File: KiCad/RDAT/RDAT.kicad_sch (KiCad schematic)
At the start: 0 parts

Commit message: Add data from KiCAD and review
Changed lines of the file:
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@@
 	)
 	(sheet
-		(at 223.52 91.44)
+		(at 125.73 55.88)
 		(size 48.26 15.24)
 		(fields_autoplaced yes)
@@
 		)
 		(property "Sheetname" "usbC_Switcher"
-			(at 223.52 90.7284 0)
+			(at 125.73 55.1684 0)
 			(effects
 				(font
@@
 		)
 		(property "Sheetfile" "C_switcher.kicad_sch"
-			(at 223.52 107.2646 0)
+			(at 125.73 71.7046 0)
 			(effects
 				(font
@@
 	)
 	(sheet
-		(at 127 78.74)
+		(at 81.28 48.26)
 		(size 30.48 25.4)
 		(fields_autoplaced yes)
@@
 		)
 		(property "Sheetname" "LattePanda_mu"
-			(at 127 78.0284 0)
+			(at 81.28 47.5484 0)
 			(effects
 				(font
@@
 		)
 		(property "Sheetfile" "mu_cm.kicad_sch"
-			(at 127 104.7246 0)
+			(at 81.28 74.2446 0)
 			(effects
 				(font
@@
 	)
 	(sheet
-		(at 76.2 54.61)
+		(at 66.04 95.25)
 		(size 12.7 5.08)
 		(fields_autoplaced yes)
@@
 		)
 		(property "Sheetname" "VRM"
-			(at 76.2 53.8984 0)
+			(at 66.04 94.5384 0)
 			(effects
 				(font
@@
 		)
 		(property "Sheetfile" "vrm.kicad_sch"
-			(at 76.2 60.2746 0)
+			(at 66.04 100.9146 0)
 			(effects
 				(font
@@
 	)
 	(sheet
-		(at 226.06 125.73)
+		(at 114.3 87.63)
 		(size 40.64 20.32)
 		(fields_autoplaced yes)
@@
 		)
 		(property "Sheetname" "BMS"
-			(at 226.06 125.0184 0)
+			(at 114.3 86.9184 0)
 			(effects
 				(font
@@
 		)
 		(property "Sheetfile" "bms.kicad_sch"
-			(at 226.06 146.6346 0)
+			(at 114.3 108.5346 0)
 			(effects
 				(font

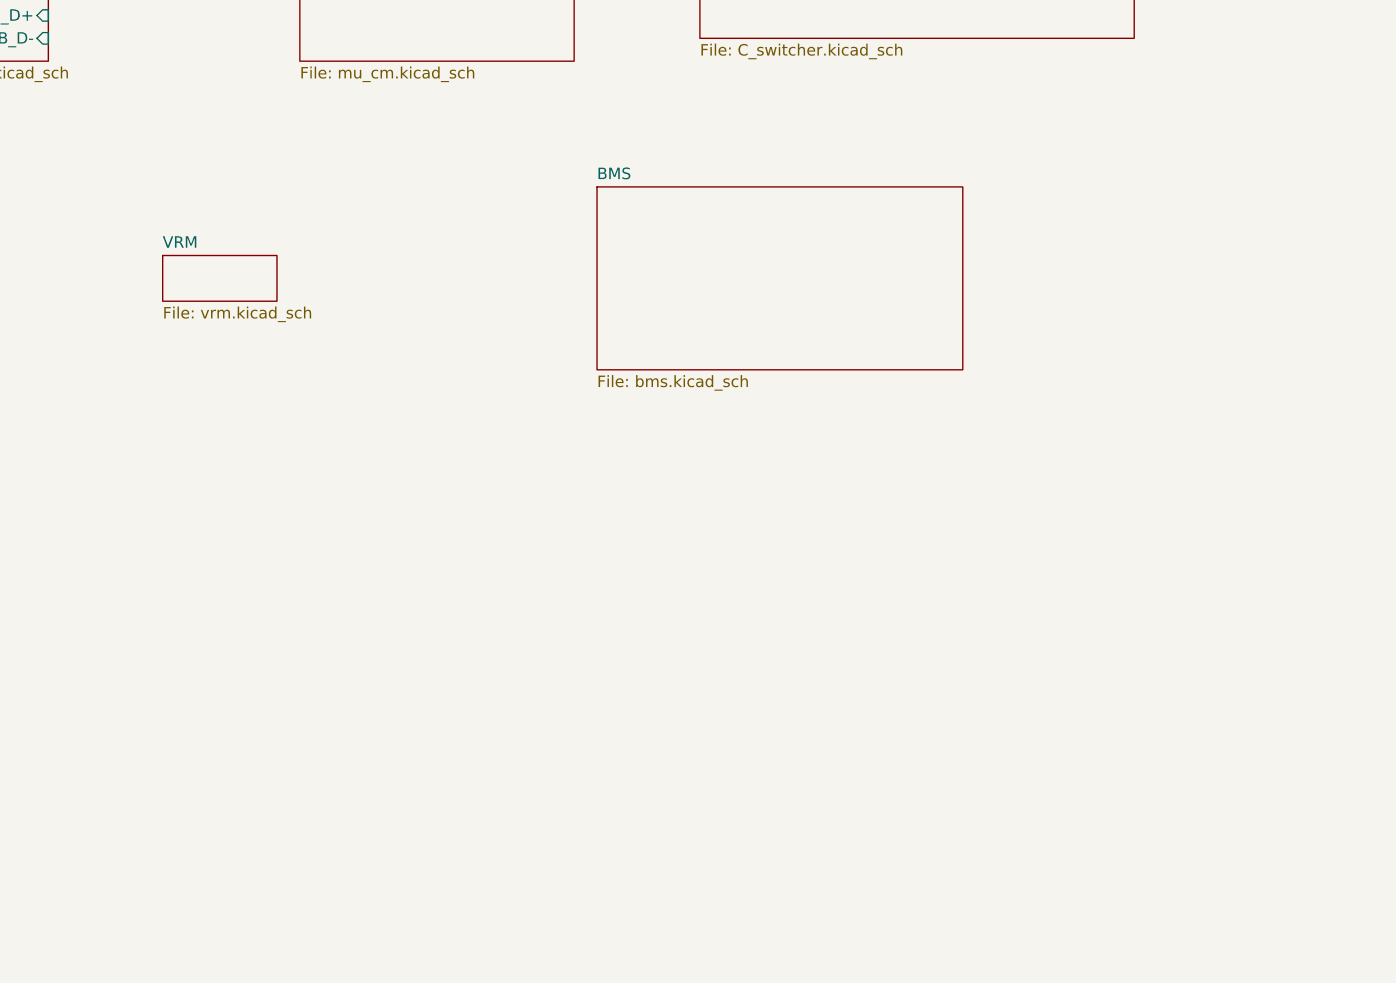
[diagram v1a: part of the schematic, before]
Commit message: BMS circuitry
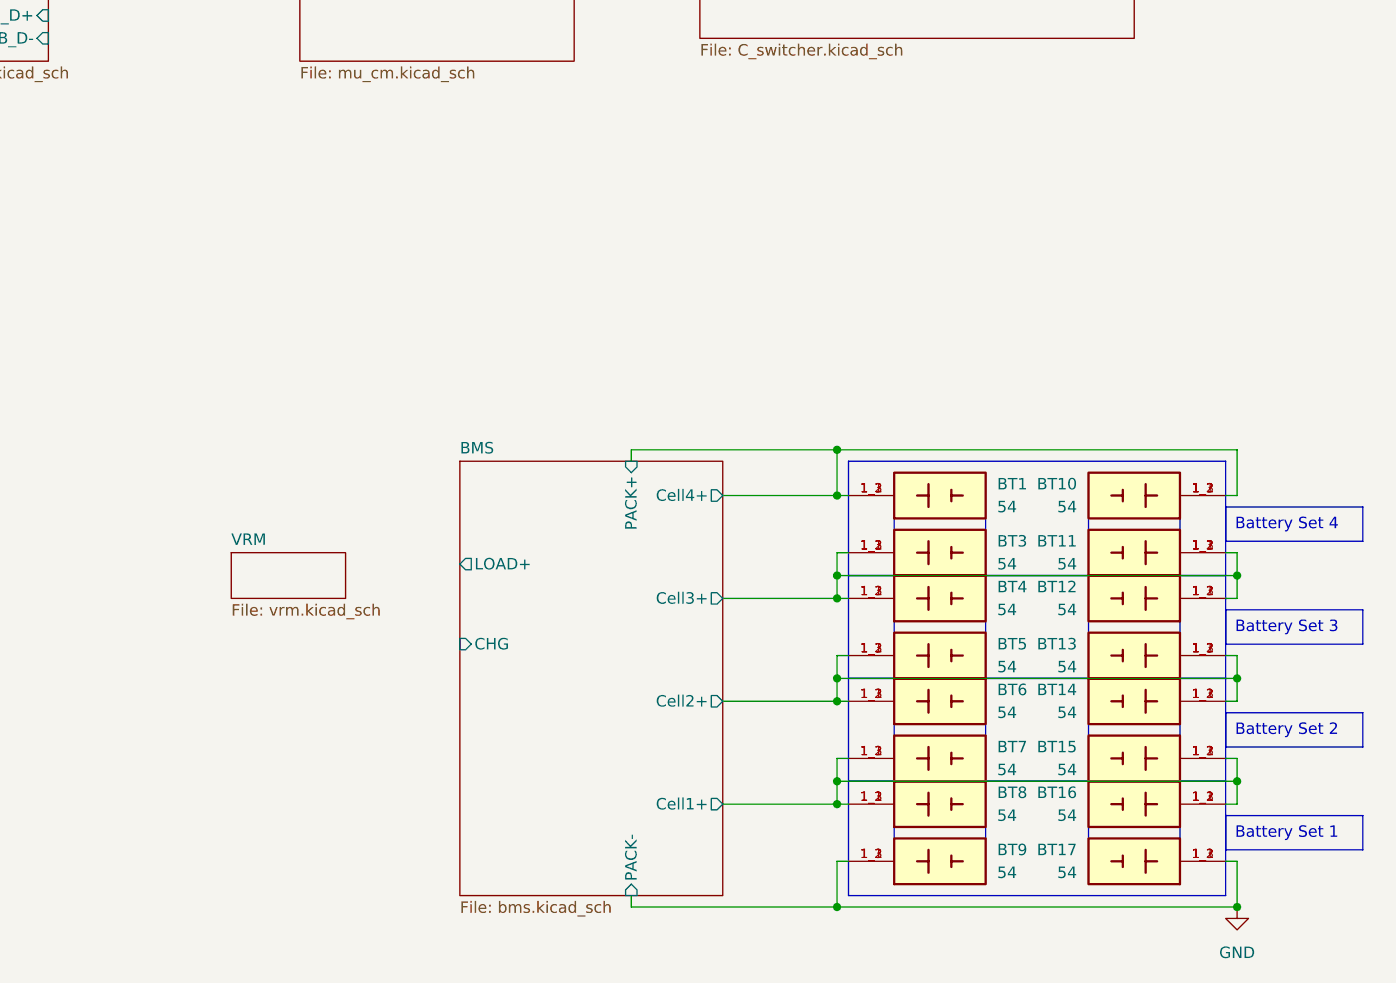
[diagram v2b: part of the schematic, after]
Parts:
- added BT1, BT10, BT11, BT12, BT13, BT14, BT15, BT16, BT17, BT3, BT4, BT5, BT6, BT7, BT8, BT9: 54, 54:BAT_54, symbol 54:54
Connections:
- new net BMS/Cell1+: BT15.1_1, BT15.1_2, BT15.1_3, BT16.1_1, BT16.1_2, BT16.1_3, BT7.1_1, BT7.1_2, BT7.1_3, BT8.1_1, BT8.1_2, BT8.1_3
- new net BMS/Cell2+: BT13.1_1, BT13.1_2, BT13.1_3, BT14.1_1, BT14.1_2, BT14.1_3, BT5.1_1, BT5.1_2, BT5.1_3, BT6.1_1, BT6.1_2, BT6.1_3
- new net BMS/Cell3+: BT11.1_1, BT11.1_2, BT11.1_3, BT12.1_1, BT12.1_2, BT12.1_3, BT3.1_1, BT3.1_2, BT3.1_3, BT4.1_1, BT4.1_2, BT4.1_3
- new net BMS/Cell4+: BT1.1_1, BT1.1_2, BT1.1_3, BT10.1_1, BT10.1_2, BT10.1_3
- new net GND: BT17.1_1, BT17.1_2, BT17.1_3, BT9.1_1, BT9.1_2, BT9.1_3
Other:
- sheet BMS ports: added CHG, Cell1+, Cell2+, Cell3+, Cell4+, LOAD+, PACK+, PACK-; removed none

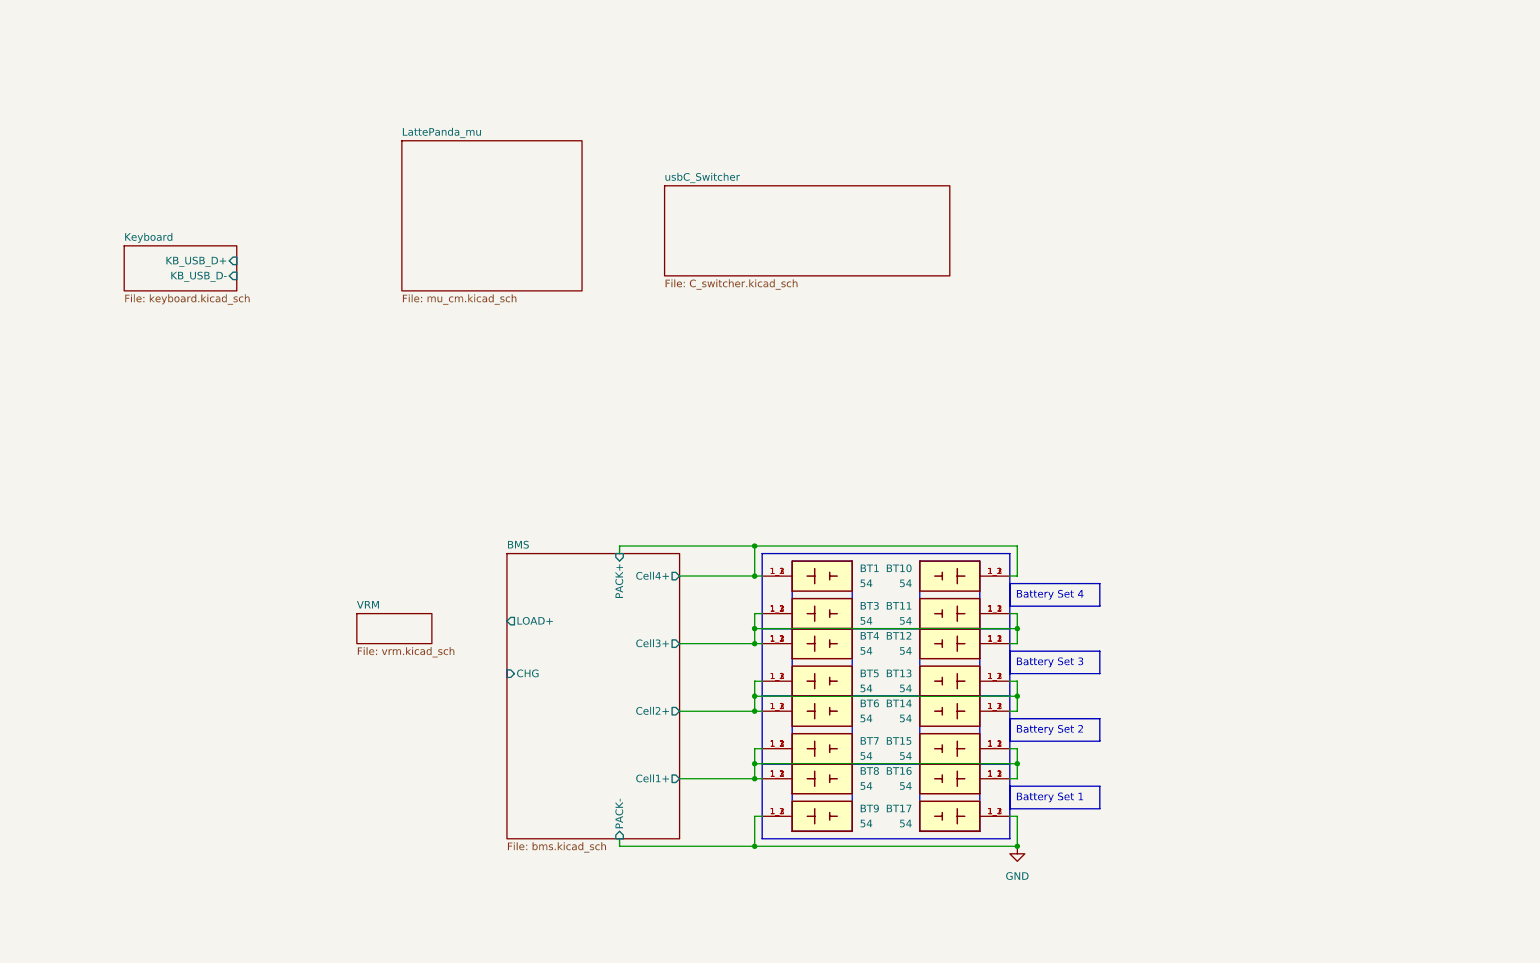
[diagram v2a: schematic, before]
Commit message: Added kicad USBC controller and connected VBUS
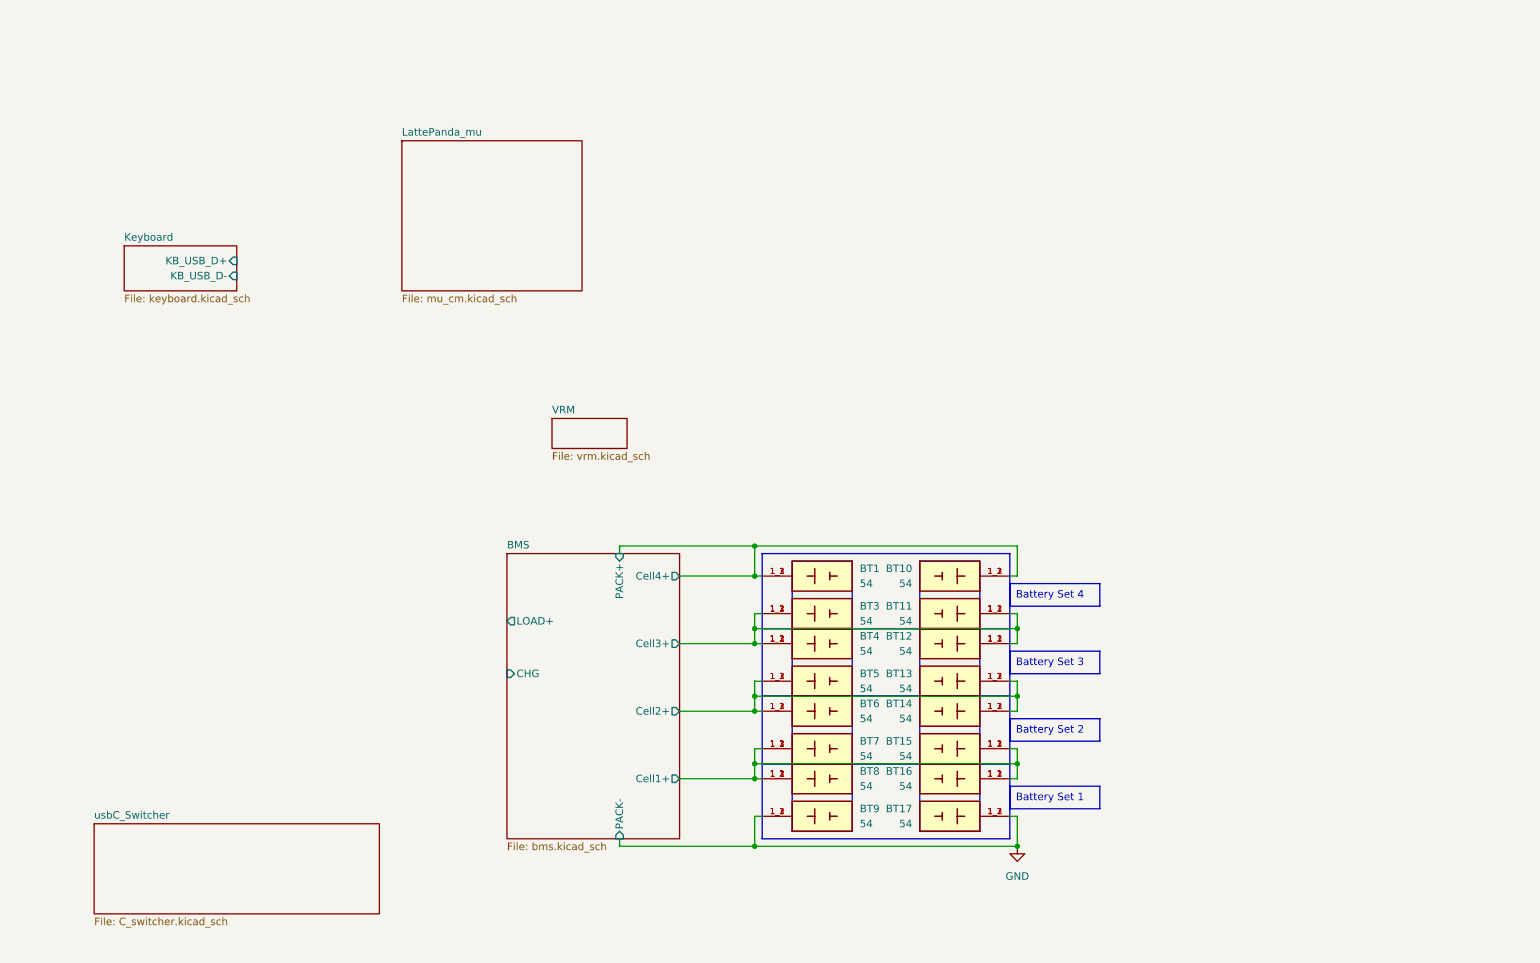
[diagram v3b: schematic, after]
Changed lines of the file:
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@@
 	)
 	(sheet
-		(at 125.73 55.88)
+		(at 29.21 163.83)
 		(size 48.26 15.24)
 		(fields_autoplaced yes)
@@
 		)
 		(property "Sheetname" "usbC_Switcher"
-			(at 125.73 55.1684 0)
+			(at 29.21 163.1184 0)
 			(effects
 				(font
@@
 		)
 		(property "Sheetfile" "C_switcher.kicad_sch"
-			(at 125.73 71.7046 0)
+			(at 29.21 179.6546 0)
 			(effects
 				(font
@@
 	)
 	(sheet
-		(at 73.66 128.27)
+		(at 106.68 95.25)
 		(size 12.7 5.08)
 		(fields_autoplaced yes)
@@
 		)
 		(property "Sheetname" "VRM"
-			(at 73.66 127.5584 0)
+			(at 106.68 94.5384 0)
 			(effects
 				(font
@@
 		)
 		(property "Sheetfile" "vrm.kicad_sch"
-			(at 73.66 133.9346 0)
+			(at 106.68 100.9146 0)
 			(effects
 				(font

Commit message: Update BMS
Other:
- added sheet m.2_B_Key (B_key.kicad_sch)
- added sheet m.2_E_Key (E_Key.kicad_sch)
- sheet usbC_Switcher ports: added POWER CHARGER OUTPUT, VIN_3V3; removed none
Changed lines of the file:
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@@
 		)
 	)
+	(text_box "power output can be 5v 9v 15v or 20v"
+		(exclude_from_sim no)
+		(at 60.96 153.67 0)
+		(size 25.4 7.62)
+		(stroke
+			(width 0)
+			(type default)
+		)
+		(fill
+			(type none)
+		)
+		(effects
+			(font
+				(size 1.27 1.27)
+			)
+			(justify left top)
+		)
+	)
 	(text_box "Battery Set 3\n"
 		(exclude_from_sim no)
@@
 	)
 	(sheet
-		(at 34.29 66.04)
+		(at 64.77 29.21)
+		(size 22.86 15.24)
+		(fields_autoplaced yes)
+		(stroke
+			(width 0.1524)
+			(type solid)
+		)
+		(fill
+			(color 0 0 0 0.0000)
+		)
+		(property "Sheetname" "m.2_E_Key"
+			(at 64.77 28.4984 0)
+			(effects
+				(font
+					(size 1.27 1.27)
+				)
+				(justify left bottom)
+			)
+		)
+		(property "Sheetfile" "E_Key.kicad_sch"
+			(at 64.77 45.0346 0)
+			(effects
+				(font
+					(size 1.27 1.27)
+				)
+				(justify left top)
+			)
+		)
+		(instances
+			(project "RDAT"
+				(path "/0db9370a-8a21-4fd2-83a9-f207c3725dc9"
+					(page "7")
+				)
+			)
+		)
+	)
+	(sheet
+		(at 102.87 91.44)
 		(size 19.05 7.62)
 		(fields_autoplaced yes)
@@
 		)
 		(property "Sheetname" "Keyboard"
-			(at 34.29 65.3284 0)
+			(at 102.87 90.7284 0)
 			(effects
 				(font
@@
 		)
 		(property "Sheetfile" "keyboard.kicad_sch"
-			(at 34.29 74.2446 0)
+			(at 102.87 99.6446 0)
 			(effects
 				(font
@@
 		)
 		(pin "KB_USB_D-" input
-			(at 53.34 71.12 0)
+			(at 121.92 96.52 0)
 			(effects
 				(font
@@
 		)
 		(pin "KB_USB_D+" input
-			(at 53.34 68.58 0)
+			(at 121.92 93.98 0)
 			(effects
 				(font
@@
 	)
 	(sheet
-		(at 29.21 163.83)
-		(size 48.26 15.24)
+		(at 17.78 120.65)
+		(size 26.67 19.05)
 		(fields_autoplaced yes)
 		(stroke
@@
 		)
 		(property "Sheetname" "usbC_Switcher"
-			(at 29.21 163.1184 0)
+			(at 17.78 119.9384 0)
 			(effects
 				(font
@@
 		)
 		(property "Sheetfile" "C_switcher.kicad_sch"
-			(at 29.21 179.6546 0)
+			(at 17.78 140.2846 0)
 			(effects
 				(font
@@
 			)
 		)
+		(pin "POWER CHARGER OUTPUT" output
+			(at 44.45 137.16 0)
+			(effects
+				(font
+					(size 1.27 1.27)
+				)
+				(justify right)
+			)
+		)
+		(pin "VIN_3V3" input
+			(at 44.45 125.73 0)
+			(effects
+				(font
+					(size 1.27 1.27)
+				)
+				(justify right)
+			)
+		)
 		(instances
 			(project "RDAT"
@@
 	)
 	(sheet
-		(at 81.28 48.26)
+		(at 87.63 29.21)
+		(size 20.32 15.24)
+		(fields_autoplaced yes)
+		(stroke
+			(width 0.1524)
+			(type solid)
+		)
+		(fill
+			(color 0 0 0 0.0000)
+		)
+		(property "Sheetname" "m.2_B_Key"
+			(at 87.63 28.4984 0)
+			(effects
+				(font
+					(size 1.27 1.27)
+				)
+				(justify left bottom)
+			)
+		)
+		(property "Sheetfile" "B_key.kicad_sch"
+			(at 87.63 45.0346 0)
+			(effects
+				(font
+					(size 1.27 1.27)
+				)
+				(justify left top)
+			)
+		)
+		(instances
+			(project "RDAT"
+				(path "/0db9370a-8a21-4fd2-83a9-f207c3725dc9"
+					(page "8")
+				)
+			)
+		)
+	)
+	(sheet
+		(at 55.88 81.28)
 		(size 30.48 25.4)
 		(fields_autoplaced yes)
@@
 		)
 		(property "Sheetname" "LattePanda_mu"
-			(at 81.28 47.5484 0)
+			(at 55.88 80.5684 0)
 			(effects
 				(font
@@
 		)
 		(property "Sheetfile" "mu_cm.kicad_sch"
-			(at 81.28 74.2446 0)
+			(at 55.88 107.2646 0)
 			(effects
 				(font
@@
 	)
 	(sheet
-		(at 106.68 95.25)
+		(at 66.04 128.27)
 		(size 12.7 5.08)
 		(fields_autoplaced yes)
@@
 		)
 		(property "Sheetname" "VRM"
-			(at 106.68 94.5384 0)
+			(at 66.04 127.5584 0)
 			(effects
 				(font
@@
 		)
 		(property "Sheetfile" "vrm.kicad_sch"
-			(at 106.68 100.9146 0)
+			(at 66.04 133.9346 0)
 			(effects
 				(font
